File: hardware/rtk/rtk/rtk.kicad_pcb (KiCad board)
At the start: 2 copper layers, 76 parts, among them J1 USB4105-GF-A, J10 Conn_01x02_Pin, J11 Conn_01x06_Pin, J2 USB4105-GF-A, J3 B2B-PH-SM4-TBLFSN, J5 Conn_Coaxial, J6 MEM2052-00-195-00-A_REVA, J7 Conn_01x04_Pin, J8 Conn_01x01_Pin, J9 Conn_01x08_Pin, U1 BQ24075RGT, U2 TPS63020DSJR, U3 STM32F765VITx, U4 ZED-F9H-01B, U5 ESP32-S3-ZERO, U6 CORE1262-868M, U7 LSM6DSOX, U8 USB3300-EZK, Y1 ASTX-H11-16.000MHZ-T, Y2 ASTX-H11-24.000MHZ-T

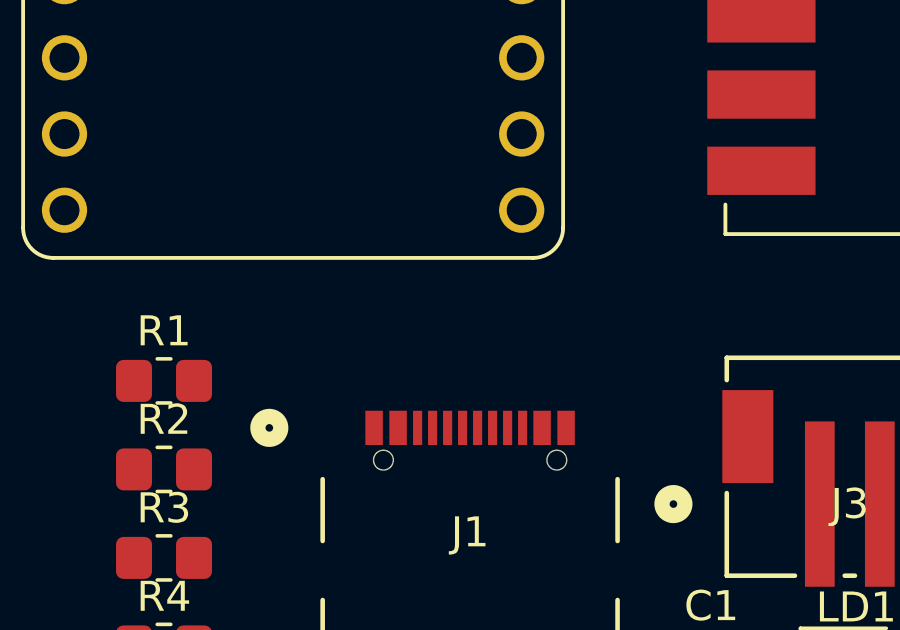
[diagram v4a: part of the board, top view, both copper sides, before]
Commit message: USB2HS sheet review fixes; ZED-F9P and misc updates (#182)
- usb2hs.kicad_sch: CPEN tied to GND, VDD1.8 caps changed to 470nF,
  PRTR5V0U2X ESD TVS added on USB_D+/D-, MMC5603NJ connector added
- stm32f765vit.kicad_sch: ESP32 GP1-GP5 wired to PE2-PE6
- docs/reference/psu/README.md: PRTR5V0U2X ESD TVS entry added

Co-Authored-By: Claude Sonnet 4.6 <noreply@anthropic.com>
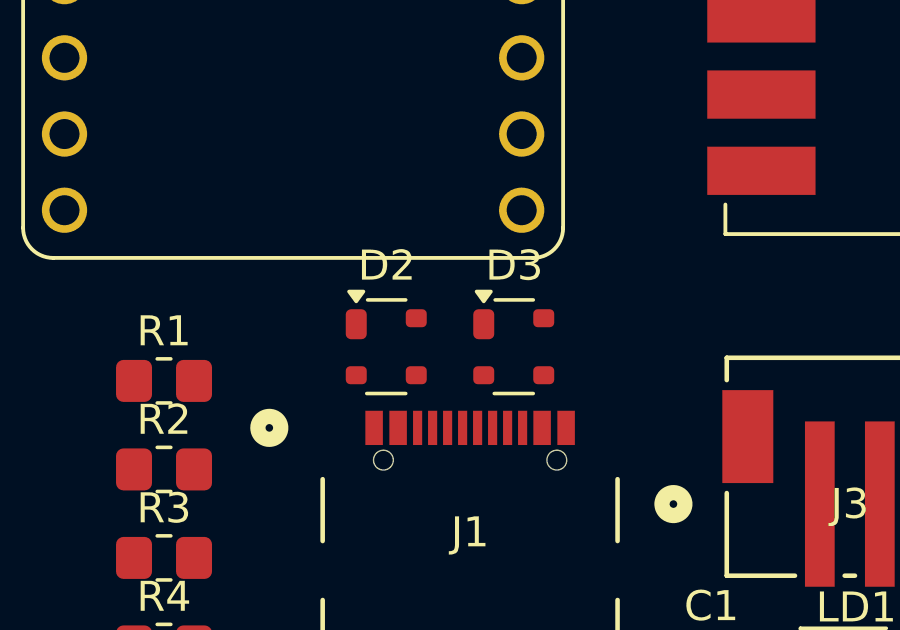
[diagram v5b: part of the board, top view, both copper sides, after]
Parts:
- added D2: PRTR5V0U2X, Package_TO_SOT_SMD:SOT-143, F.Cu at (95.6, 83.8)
- added D3: PRTR5V0U2X, Package_TO_SOT_SMD:SOT-143, F.Cu at (99.9, 83.8)
- C28, C29: value 100n -> 470n
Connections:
- J1 pad A6: USB_D_P -> USB_D2_P
- J1 pad A7: USB_D_N -> USB_D2_N
- J1 pad B6: USB_D_P -> USB_D2_P
- J1 pad B7: USB_D_N -> USB_D2_N
- U8 pad 3: unconnected-(U8-CPEN-Pad3) -> GND

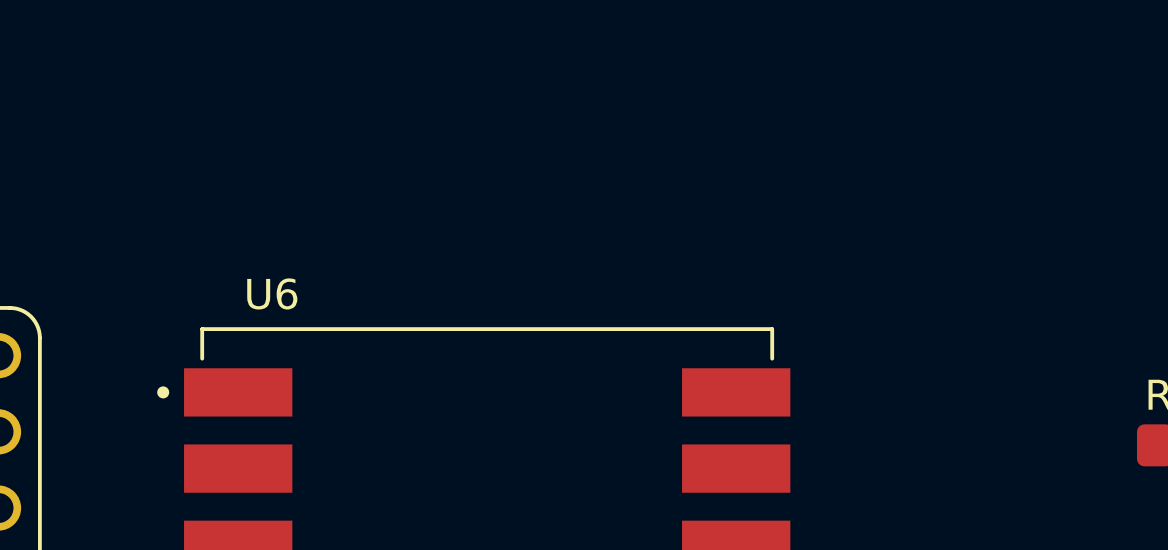
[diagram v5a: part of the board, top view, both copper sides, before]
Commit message: ZED-F9P sheet review fixes (#182)
- V_BCKP tied to +3V3 with 100nF decoupling
- VCC decoupling caps added on module side of L2/L3
- SAFEBOOT_N and RESET_N 10k pull-ups to +3V3 added
- L3 on VCC_RF replaced with ferrite bead (600R at 100MHz)

Co-Authored-By: Claude Sonnet 4.6 <noreply@anthropic.com>
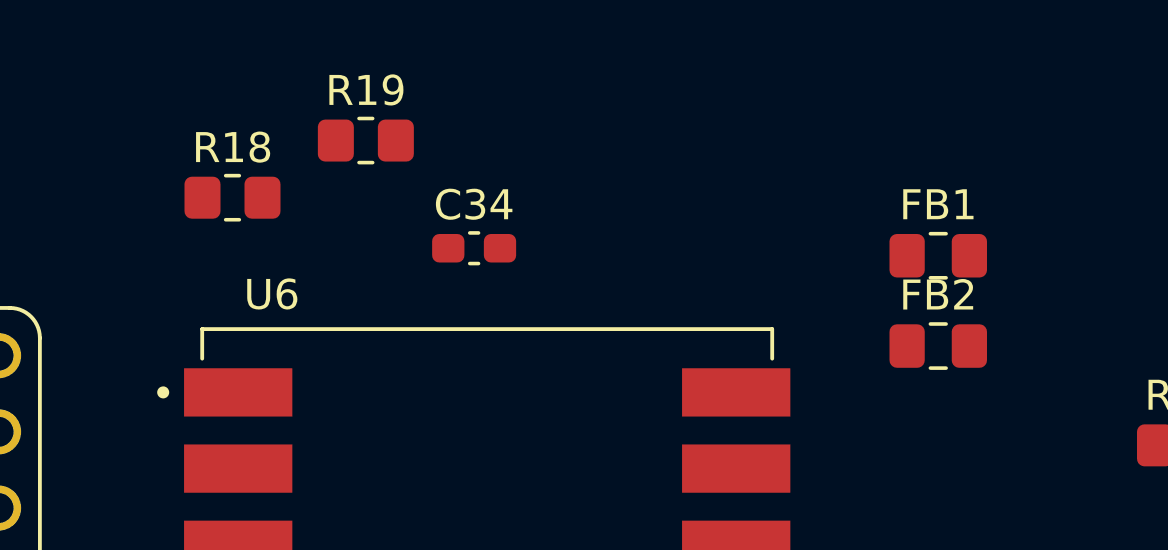
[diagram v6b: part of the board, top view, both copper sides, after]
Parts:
- added C34: 100n, Capacitor_SMD:C_0603_1608Metric_Pad1.08x0.95mm_HandSolder, F.Cu at (116.0, 55.4)
- added FB1: FerriteBead_Small, Capacitor_SMD:C_0805_2012Metric_Pad1.18x1.45mm_HandSolder, F.Cu at (131.4, 55.6)
- added FB2: FerriteBead_Small, Capacitor_SMD:C_0805_2012Metric_Pad1.18x1.45mm_HandSolder, F.Cu at (131.4, 58.6)
- added R18: 10k, Resistor_SMD:R_0805_2012Metric_Pad1.20x1.40mm_HandSolder, F.Cu at (107.9, 53.7)
- added R19: 10k, Resistor_SMD:R_0805_2012Metric_Pad1.20x1.40mm_HandSolder, F.Cu at (112.4, 51.8)
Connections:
- U4 pad 36: unconnected-(U4A-V_BCKP-Pad36) -> +3V3

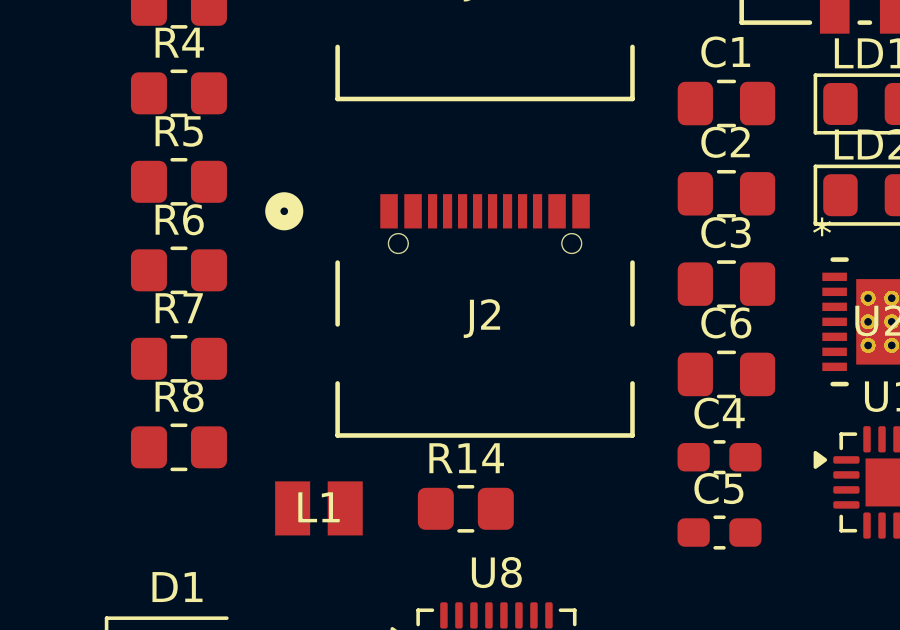
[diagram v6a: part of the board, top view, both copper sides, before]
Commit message: Full schematic review complete — final fixes (#182)
- power.kicad_sch: J2 USB-C removed (J1 covers both power and data),
  CC1/CC2 5k1 pull-downs on J1 confirmed
- usb2hs.kicad_sch: VDD1.8 decoupling updated to 470nF, ESD TVS added
- stm32f765vit.kicad_sch: misc cleanup from review
- zed-f9p-05b.kicad_sch: V_BCKP, decoupling, pull-ups, ferrite bead fixes

Co-Authored-By: Claude Sonnet 4.6 <noreply@anthropic.com>
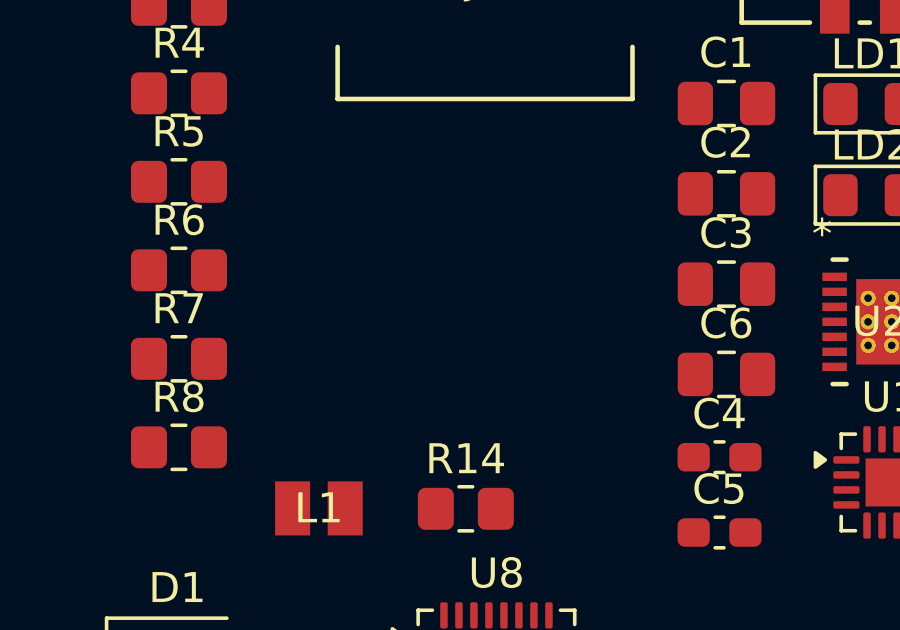
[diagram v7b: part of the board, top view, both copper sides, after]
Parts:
- removed J2: USB4105-GF-A, USB4105-GF-A-060:USB4105_GCT

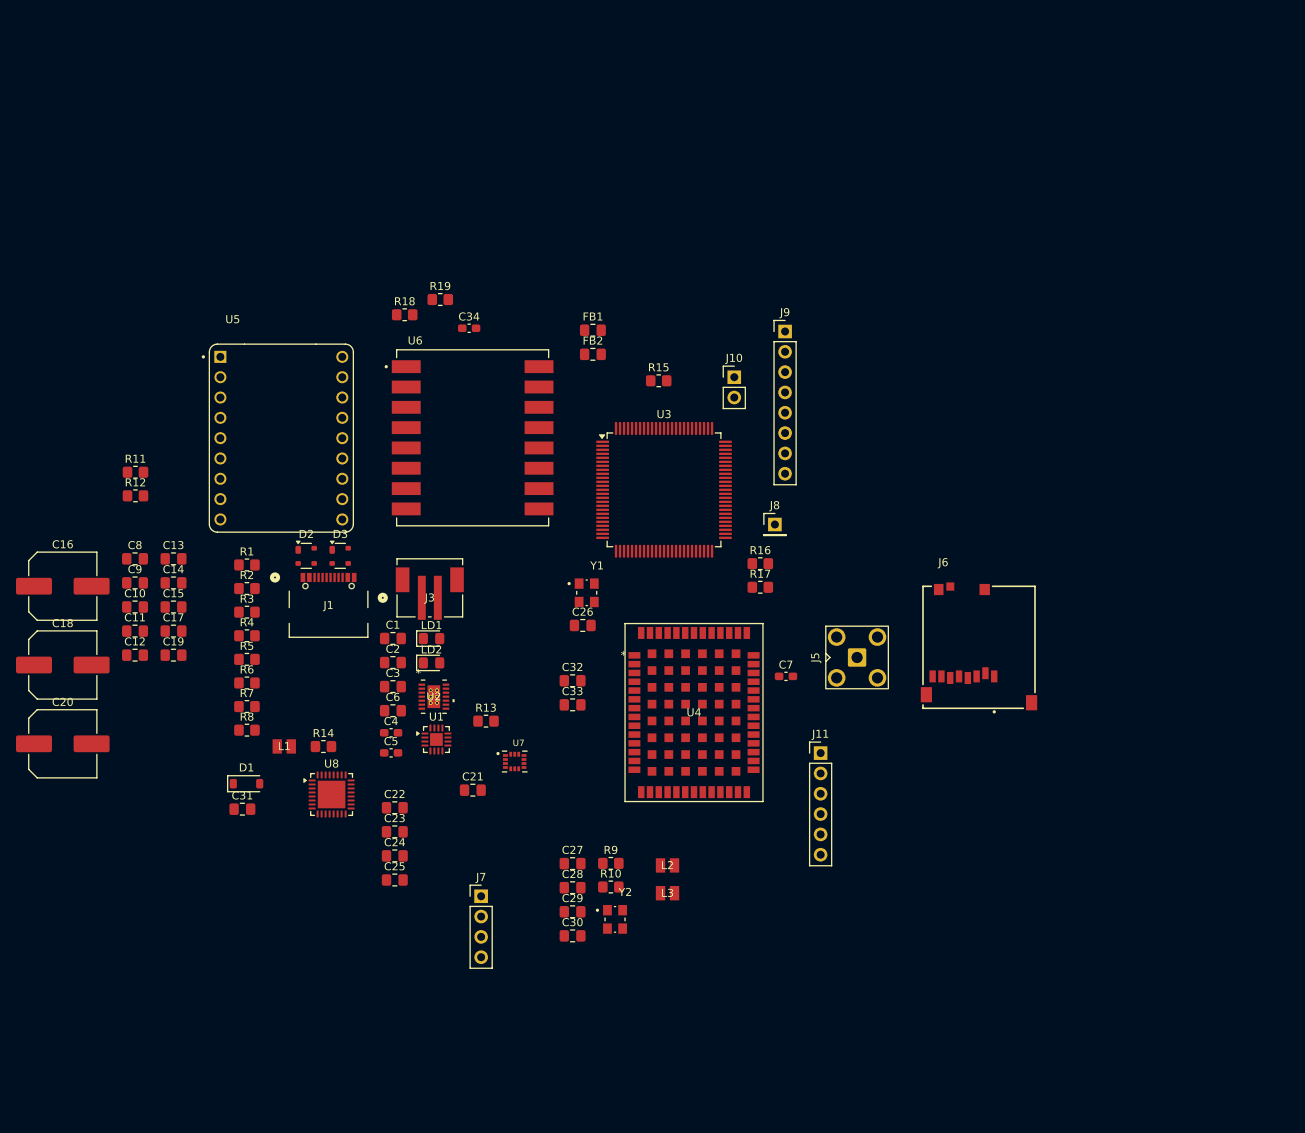
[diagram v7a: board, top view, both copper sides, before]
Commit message: Schematic fixes and PCB placement start: D2, C16/18/20, J4
- D2: PRTR5V0U2X → USBLC6-2SC6 (SOT-23-6), D3 removed
- C16/C18/C20: symbol → C_Polarized_Small, footprint → 0805 HandSolder
  (T529P106M010AAE200 polymer tant 10µF 10V)
- J4: footprint assigned (PinHeader 2.54mm, on/off switch)
- rtk.kicad_pcb: initial component placement begun
- Add USBLC6-2SC6 datasheet

Co-Authored-By: Claude Sonnet 4.6 <noreply@anthropic.com>
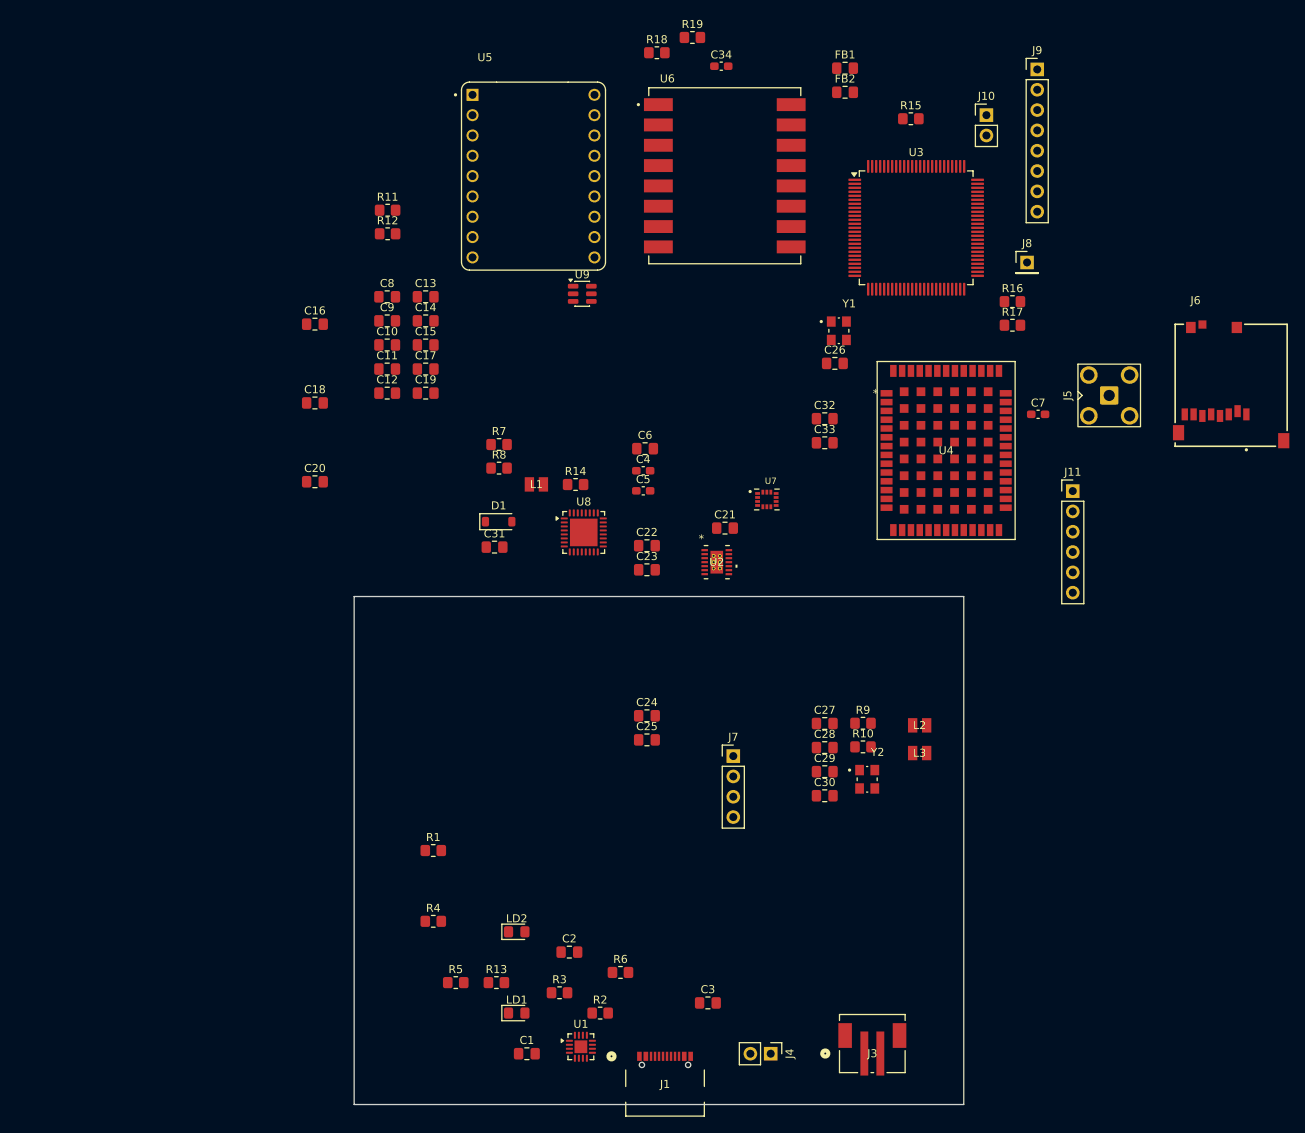
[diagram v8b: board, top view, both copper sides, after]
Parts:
- removed D2, D3: PRTR5V0U2X, Package_TO_SOT_SMD:SOT-143
- added J4: Conn_01x02_Pin, Connector_PinHeader_2.54mm:PinHeader_1x02_P2.54mm_Vertical, F.Cu at (153.7, 146.1)
- added U9: USBLC6-2SC6, Package_TO_SOT_SMD:SOT-23-6, F.Cu at (130.1, 51.1)
- C16, C18, C20: footprint Capacitor_SMD:C_Elec_8x10.2 -> Capacitor_SMD:C_0805_2012Metric_Pad1.18x1.45mm_HandSolder
- moved J3 79.4 mm to (166.4, 144.8)
- moved J1 73.2 mm to (140.5, 149.9)
- moved R2 69.0 mm to (132.3, 141.0)
- moved R3 61.6 mm to (127.3, 138.4)
- moved R6 59.1 mm to (134.9, 135.9)
- moved C3 55.8 mm to (145.8, 139.7)
- moved C1 54.5 mm to (123.2, 146.1)
- moved R5 48.1 mm to (114.3, 137.2)
- moved LD1 48.0 mm to (121.9, 141.0)
- moved C21 45.5 mm to (148.0, 80.3)
- moved C32 45.5 mm to (160.4, 66.7)
- moved C31 45.5 mm to (119.1, 82.7)
- moved L1 45.5 mm to (124.4, 74.9)
- moved R8 45.5 mm to (119.7, 72.8)
- moved U7 45.5 mm to (153.2, 76.8)
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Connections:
- U3 pad 81: unconnected-(U3-PD0-Pad81) -> BQ24975_nCE
- U3 pad 84: unconnected-(U3-PD3-Pad84) -> BQ24975_EN1
- U3 pad 85: unconnected-(U3-PD4-Pad85) -> BQ24975_EN2
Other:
- board outline added: 76.2 x 63.5 mm
